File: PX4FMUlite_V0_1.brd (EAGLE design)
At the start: 70 x 40.5 mm, 192 parts, among them J201 DF13C-6P-1.25V, J202 DF13C-6P-1.25V, J203 DF13C-6P-1.25V, J204 DF13C-6P-1.25V, J301 47346-0001, J302 DF13C-4P-1.25V, J401 DF13C-4P-1.25V, J403 DF13C-7P-1.25V, J404 DF13C-5P-1.25V, J405 DF13C-4P-1.25V, J601 DF13C-6P-1.25V, J702 DF13C-3P-1.25V, J801 JST-ZH-3, M3_MOUNT1101 MOUNT-HOLE3.1MM, M3_MOUNT1102 MOUNT-HOLE3.1MM, M3_MOUNT1103 MOUNT-HOLE3.1MM, M3_MOUNT1104 MOUNT-HOLE3.1MM, U101 STM32F4X7VX, U102 FM25V01, U201 TXS0108QFN20, U202 TXS0108QFN20, U301 2908-05WB-MG, U401 MAX3051, U502 L3GD20H, U503 MS5611-01BA, U701 TCA62724FMG, U703 LRTB GFTG-T7AW-1+V7A7-29+R5T9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, U901 TXS0108QFN20, U903 74LVC2G240, X101 3.2x2.5 mm / 24 MHz / 15 ppm

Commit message: lots of ripus done on V0_1
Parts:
- moved R207 76.7 mm to (30.0, 82.0)
- moved C202 76.7 mm to (34.0, 83.6)
- moved J203 76.7 mm to (34.4, 83.6)
- moved JP2 76.7 mm to (29.0, 77.7)
- moved R214 76.7 mm to (31.2, 82.4)
- moved S3RX 76.7 mm to (31.6, 80.0)
- moved U202 76.7 mm to (34.0, 80.0)
- moved JX801 52.4 mm to (22.3, 53.5)
- moved R607 44.8 mm to (59.0, 72.0)
- moved L601 44.8 mm to (61.3, 73.2)
- moved L602 44.8 mm to (61.3, 74.6)
- moved L603 44.8 mm to (59.5, 68.8)
- moved R604 44.8 mm to (59.0, 73.2)
- moved R605 44.8 mm to (59.0, 74.6)
- moved R606 44.8 mm to (59.0, 70.9)
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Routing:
- net GNDX: track 96.4 -> 25.2 mm, vias 15 -> 0
- net VBUS: track 57.3 -> 0.10 mm, vias 4 -> 0
- net !GYRO_CS: track 56.8 -> 0.00 mm, vias 1 -> 0
- net ACCEL_DRDY: track 52.6 -> 0.00 mm, vias 2 -> 0
- net !BARO_CS: track 47.6 -> 0.00 mm, vias 1 -> 0
- net FMU-VDD_3V3: track 71.3 -> 24.7 mm, vias 10 -> 0
- net FMU-!RESET: track 45.7 -> 1.94 mm, vias 3 -> 0
- net GPIO_EXT_1: track 42.2 -> 0.10 mm, vias 2 -> 0
- net SPI_INT_SCK: track 43.7 -> 2.07 mm, vias 1 -> 0
- net BATT_VOLTAGE_SENS: track 42.2 -> 0.66 mm, vias 2 -> 0
- net SPI_EXT_SCK: track 41.4 -> 0.00 mm, vias 3 -> 0
- net SPI_INT_MOSI: track 43.2 -> 2.14 mm, vias 1 -> 0
- net SPI_EXT_MISO: track 40.5 -> 0.00 mm, vias 3 -> 0
- net SPI_INT_MISO: track 41.5 -> 1.28 mm, vias 1 -> 0
- net !SPI_EXT_NSS: track 40.0 -> 0.00 mm, vias 3 -> 0
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- removed copper zone on layer 15, net FMU-VDD_3V3
- removed copper zone on layer 16, net GNDX
- removed copper zone on layer 16, net RGB_LED_14
- removed copper zone on layer 16, net RGB_LED_3
- removed copper zone on layer 16, net RGB_LED_4
- removed copper zone on layer 1, net VBUS
- removed copper zone on layer 3, net VBUS
- removed copper zone on layer 15, net VDD_3V3_SENSORS
- removed copper zone on layer 1, net VDD_5V_BRICK
- removed copper zone on layer 16, net VDD_5V_BRICK
- removed copper zone on layer 1, net VDD_5V_IN
- removed copper zone on layer 15, net VDD_5V_IN
- removed copper zone on layer 16, net VDD_5V_IN
- removed copper zone on layer 1, net VDD_5V_PERIPH
- removed copper zone on layer 15, net VDD_5V_PERIPH
- removed copper zone on layer 1, net VDD_SERVO
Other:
- board size 70 x 40.5 mm -> 70 x 34.9 mm
- board text added: "PX4FMULite V0.1"
- board text removed: "PX4FMU v2.3"

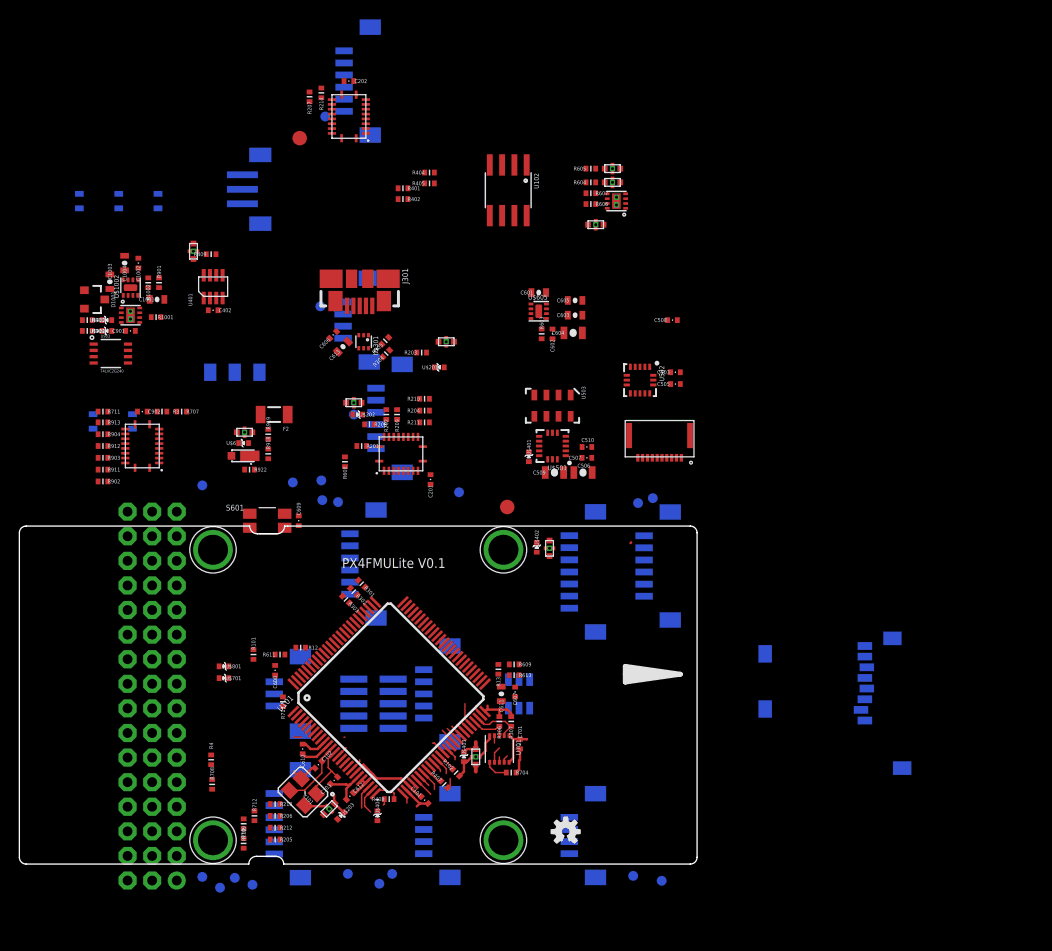
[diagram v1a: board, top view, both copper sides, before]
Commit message: Resize board, resized servo conn plus more
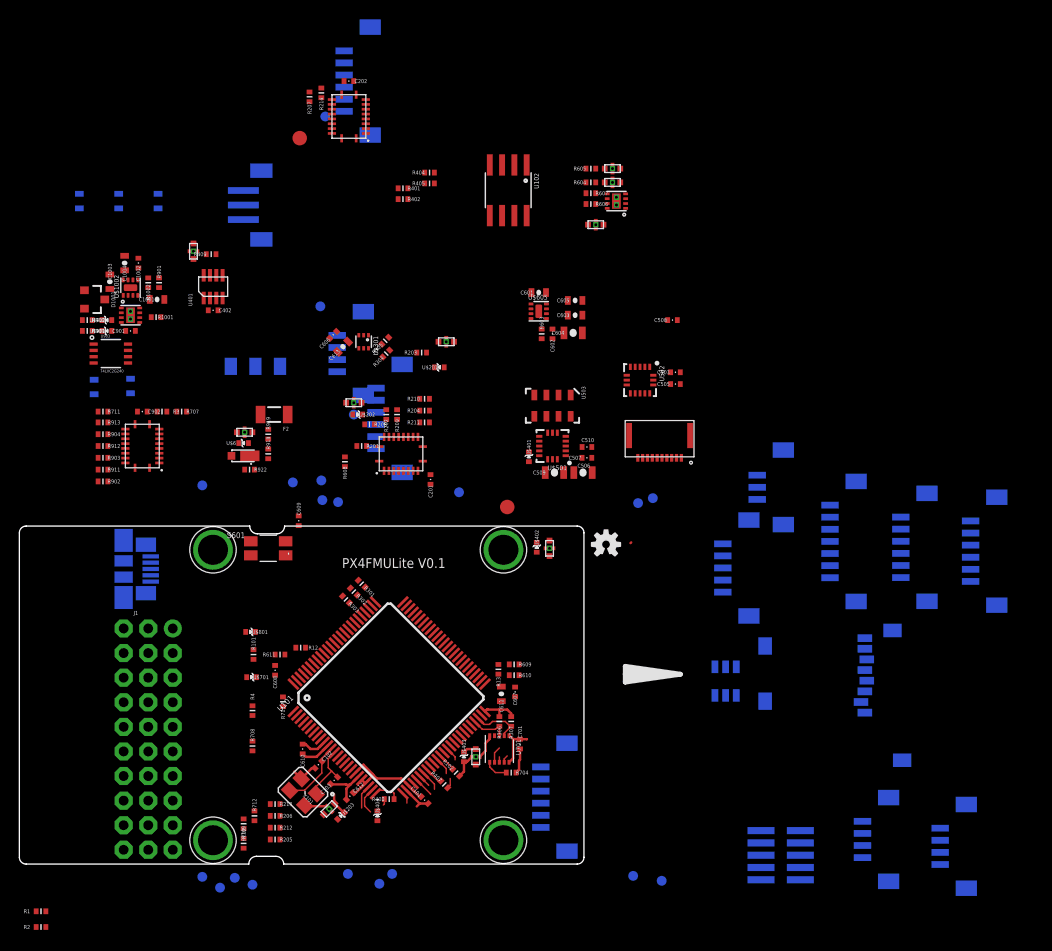
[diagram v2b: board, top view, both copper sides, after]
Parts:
- removed J901: (no value), pixhawk2:3X16RA
- added J1: (no value), PX4lite:3X10RA
- added R1, R2: 220R, pixhawk2:0402-RES
- moved J201 64.1 mm to (99.2, 35.1)
- moved J702 54.3 mm to (77.1, 41.7)
- moved J405 45.3 mm to (88.0, 5.28)
- moved JX301 44.9 mm to (78.6, 3.66)
- moved J301 38.6 mm to (10.8, 33.2), flipped to the bottom, turned to 180 degrees
- moved J401 38.3 mm to (96.0, 4.57)
- moved J404 33.5 mm to (73.6, 33.3)
- moved OSHW_LOGO 30.0 mm to (60.6, 35.8)
- moved J204 27.7 mm to (54.8, 9.65)
- moved J403 27.1 mm to (84.6, 36.1)
- moved J601 26.6 mm to (91.9, 35.5)
- moved U703 21.4 mm to (72.9, 21.6)
- moved R4 6.63 mm to (24.1, 18.6)
- moved R708 5.75 mm to (24.1, 14.9)
- moved U$801 4.49 mm to (23.9, 26.7)
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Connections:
- new net N$15: J1.22, R1.P$2
- new net N$16: J1.19, R2.P$2
- new net N$18: R1.P$1, U901.13
- new net N$21: R2.P$1, U901.12
- net FMU-CH1-PROT: now also J1.1; no longer J901.46
- net FMU-CH6-PROT: now also J1.16; no longer J901.31
- net GNDX: now also J1.12, J1.15, J1.18, J1.21, J1.24, J1.27, J1.3, J1.30, J1.6, J1.9; no longer J901.12, J901.15, J901.18, J901.21, J901.24, J901.27, J901.3, J901.30, J901.33, J901.36, J901.39, J901.42, J901.45, J901.48, J901.6, J901.9
- net IO-VDD_5V5: no longer J901.2
- net N$68: now also J1.13; no longer J901.34
- net N$77: now also J1.10; no longer J901.37
- net N$78: now also J1.7; no longer J901.40
- net N$79: now also J1.4; no longer J901.43
- net N$99: no longer J901.4
- net PPM-SBUS-PROT: no longer J901.1
- net VDD_SERVO: now also J1.11, J1.14, J1.17, J1.2, J1.20, J1.23, J1.26, J1.29, J1.5, J1.8; no longer J901.11, J901.14, J901.17, J901.20, J901.23, J901.26, J901.29, J901.32, J901.35, J901.38, J901.41, J901.44, J901.47, J901.5, J901.8
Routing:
- net !VDD_5V_PERIPH_OC: track 2.49 -> 0.00 mm
- net FMU-!RESET: track 1.94 -> 0.00 mm
- net !VDD_5V_HIPOWER_OC: track 1.75 -> 0.00 mm
- net FMU-UART7_RX: track 1.59 -> 0.00 mm
- net FMU-CH3: track 1.52 -> 0.00 mm
- net FMU_AUX_ADC1: track 2.03 -> 0.65 mm
- net !FMU-LED_AMBER: track 1.32 -> 0.00 mm
- net N$12: track 1.21 -> 0.00 mm
- net GYRO_DRDY: track 1.19 -> 0.00 mm
- net VDD_5V_SENS: track 1.18 -> 0.00 mm
- net FMU-CH2: track 1.09 -> 0.00 mm
- net FMU-CH1: track 0.87 -> 0.00 mm
- net VBAT: track 0.84 -> 0.00 mm
- net VDD_5V_PERIPH: track 0.72 -> 0.00 mm
- net N$98: track 2.07 -> 1.34 mm
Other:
- board size 70 x 34.9 mm -> 58.3 x 34.9 mm

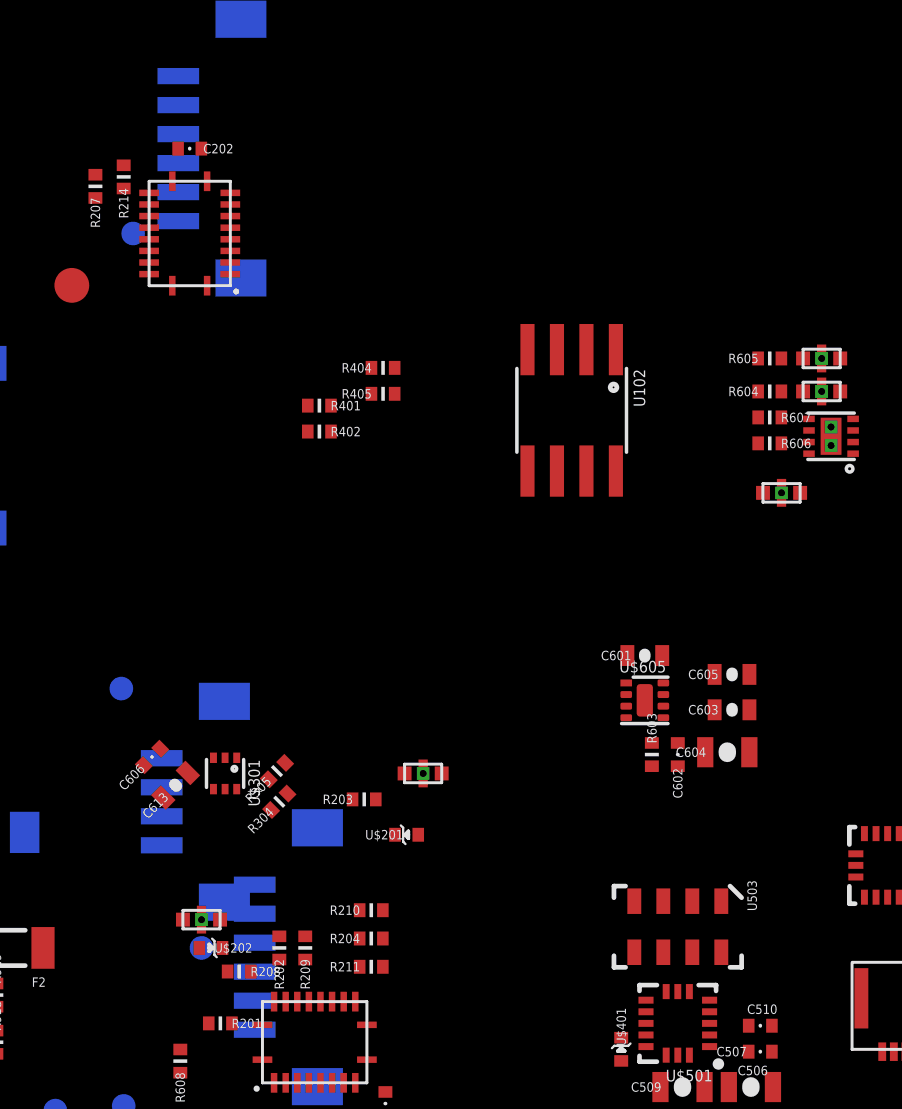
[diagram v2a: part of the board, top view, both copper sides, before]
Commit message: Removed TXS0105 buffer on excess uarts
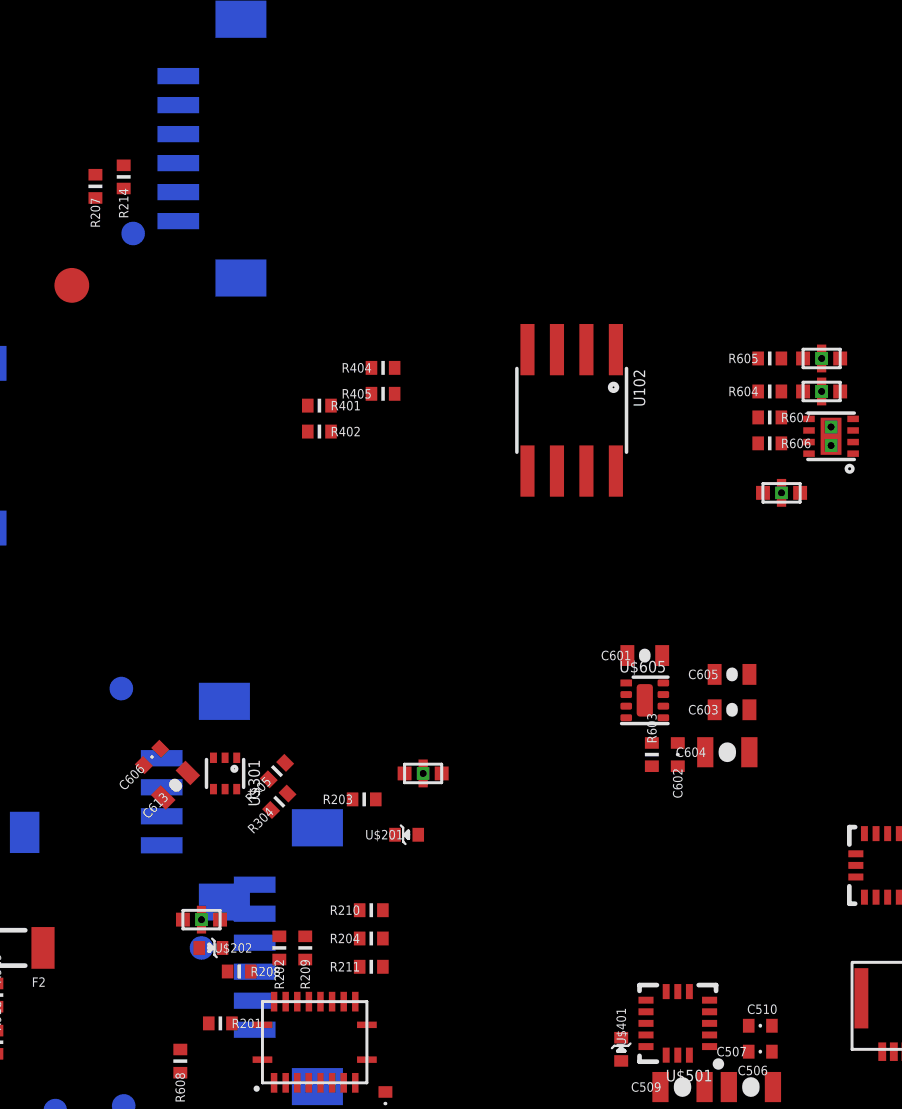
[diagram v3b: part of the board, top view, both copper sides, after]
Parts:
- removed C202: 0u1, pixhawk2:0402-CAP
- removed U202: TXS0108QFN20, pixhawk2:QFN20-RGY
- removed U503: MS5611-01BA, pixhawk2:MS5611-01BA
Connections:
- removed net N$90: R214.P$1, U202.12
- removed net N$91: R205.P$1, U202.17
- removed net N$92: R212.P$1, U202.16
- removed net N$93: R206.P$1, U202.15
- removed net N$94: R213.P$1, U202.14
- net !BARO_CS: no longer U503.5
- net FMU-UART4_RX: no longer U202.8
- net FMU-UART4_TX: now also R214.P$1; no longer U202.9
- net FMU-UART7_RX: now also R205.P$1; no longer U202.4
- net FMU-UART7_TX: now also R212.P$1; no longer U202.5
- net FMU-UART8_RX: now also R206.P$1; no longer U202.6
- net FMU-UART8_TX: now also R213.P$1; no longer U202.7
- net FMU-VDD_3V3: no longer C202.P$1, U202.10, U202.19, U202.2
- net GNDX: no longer C202.P$2, U202.11, U503.2, U503.3
- net N$89: no longer U202.13
- net SPI_INT_MISO: no longer U503.6
- net SPI_INT_MOSI: no longer U503.7
- net SPI_INT_SCK: no longer U503.8
- net VDD_3V3_SENSORS: no longer U503.1

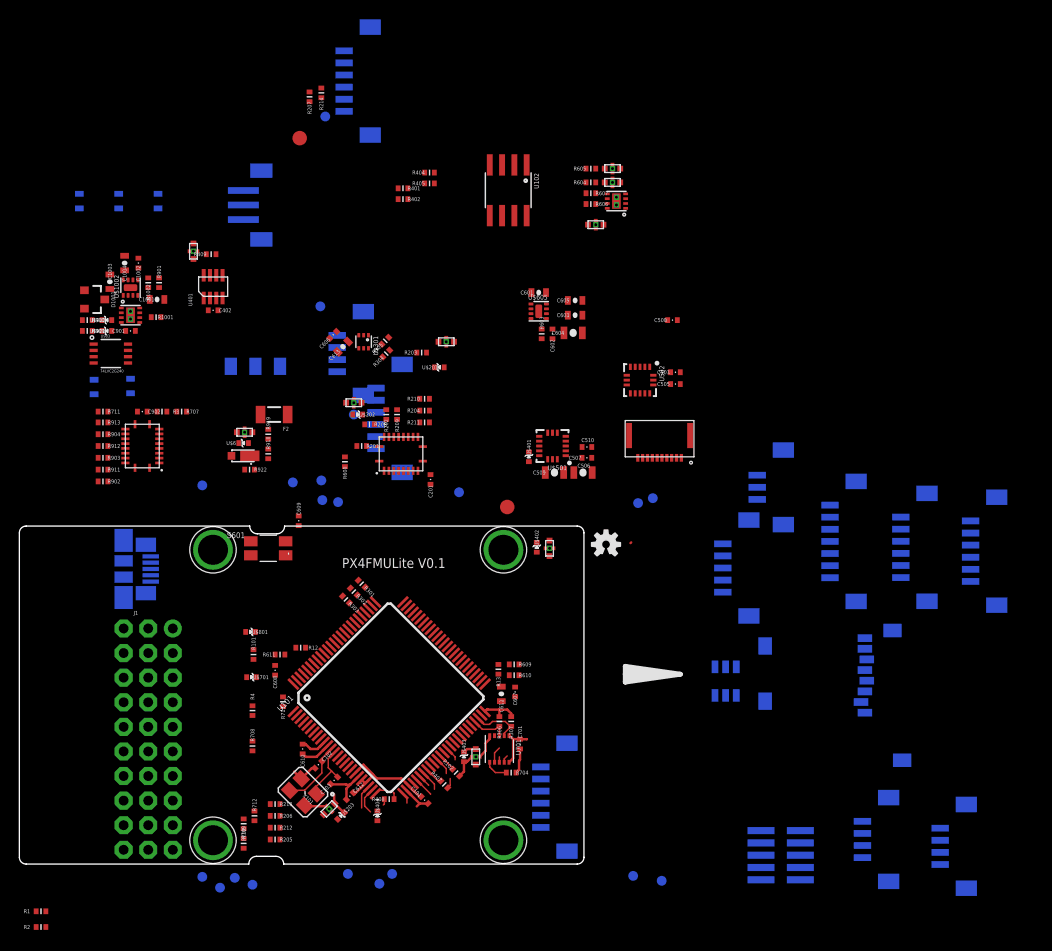
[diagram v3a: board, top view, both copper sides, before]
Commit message: Replaced lvl translators with NFU8042 ESD/EMI filters
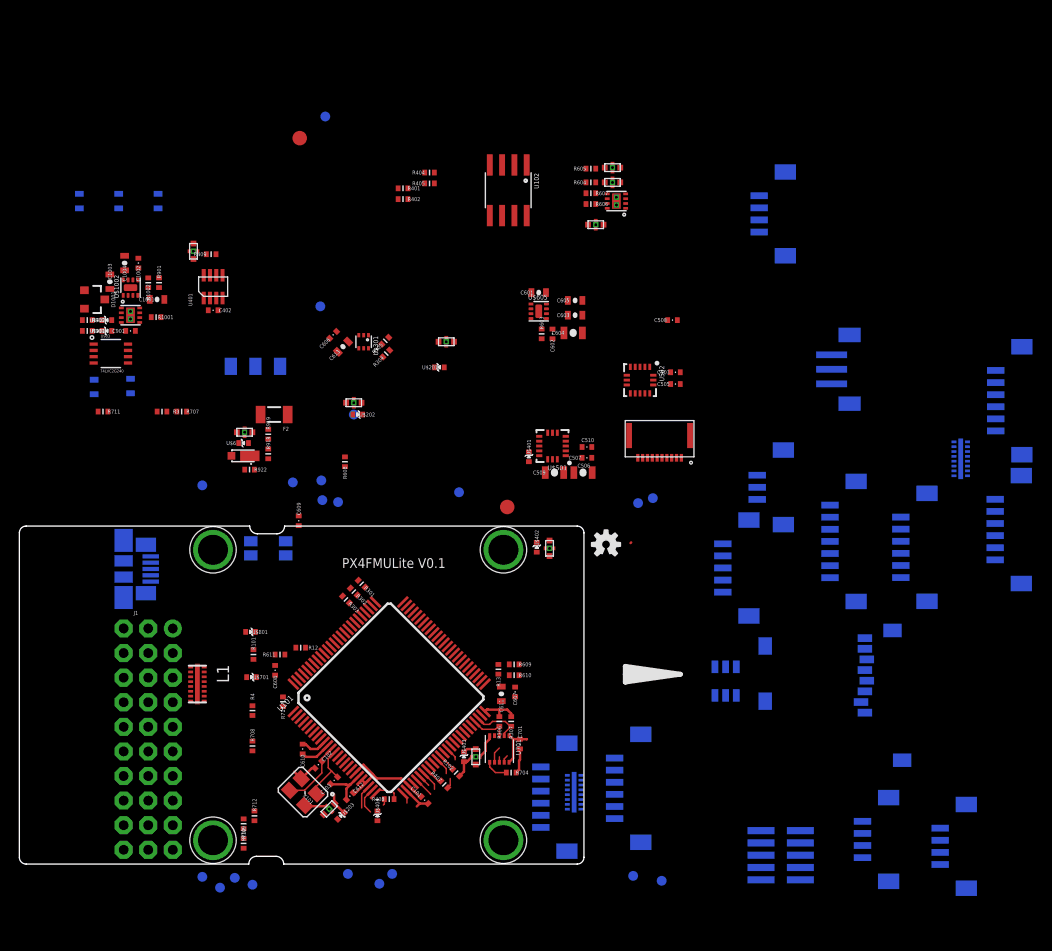
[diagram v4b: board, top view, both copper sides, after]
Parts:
- removed C201, C902: 0u1, pixhawk2:0402-CAP
- removed R1, R2, R902, R903, R904, R911, R912, R913: 220R, pixhawk2:0402-RES
- removed R201, R202, R203, R204, R205, R206, R207, R208, R209, R210, R211, R212, R213, R214: 120R, pixhawk2:0402-RES
- removed U201, U901: TXS0108QFN20, pixhawk2:QFN20-RGY
- added L1, L2, L3: NUF8402MN, PX4lite:DFN16-THIN
- moved J203 78.2 mm to (62.4, 10.6)
- moved J202 64.0 mm to (101.7, 50.6)
- moved J801 63.1 mm to (85.6, 53.8)
- moved J302 45.9 mm to (77.3, 69.9)
- moved J201 3.38 mm to (101.7, 37.3)
- moved L602 0.10 mm to (61.3, 74.7)
- flipped S601 to the bottom
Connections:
- removed net FMU-CH6-PROT: J1.16, R902.P$2
- removed net N$18: R1.P$1, U901.13
- removed net N$21: R2.P$1, U901.12
- removed net N$61: R902.P$1, U901.20
- removed net N$62: R911.P$1, U901.18
- removed net N$63: R903.P$1, U901.17
- removed net N$64: R912.P$1, U901.16
- removed net N$65: R904.P$1, U901.15
- removed net N$66: R913.P$1, U901.14
- removed net N$70: R201.P$1, U201.20
- removed net N$82: R208.P$1, U201.18
- removed net N$83: R202.P$1, U201.17
- removed net N$84: R209.P$1, U201.16
- removed net N$85: R203.P$1, U201.15
- removed net N$86: R210.P$1, U201.14
- removed net N$87: R204.P$1, U201.13
- removed net N$88: R211.P$1, U201.12
- removed net N$89: R207.P$1
- new net N$32: L1.P$7
- new net N$36: J1.16, L1.P$11
- net FMU-CH1: no longer U901.7
- net FMU-CH1-PROT: now also L1.P$16; no longer R913.P$2
- net FMU-CH2: no longer U901.6
- net FMU-CH3: no longer U901.5
- net FMU-CH4: no longer U901.4
- net FMU-CH5: no longer U901.3
- net FMU-CH6: no longer U901.1
- net FMU-UART4_RX: now also L3.P$5
- net FMU-UART4_TX: now also L3.P$6; no longer R214.P$1
- net FMU-UART7_RX: now also L3.P$1; no longer R205.P$1
- net FMU-UART7_TX: now also L3.P$2; no longer R212.P$1
- net FMU-UART8_RX: now also L3.P$3; no longer R206.P$1
- net FMU-UART8_TX: now also L3.P$4; no longer R213.P$1
- net FMU-USART2_CTS: now also L2.P$8; no longer U201.9
- net FMU-USART2_RTS: now also L2.P$7; no longer U201.8
- net FMU-USART2_RX: now also L2.P$5; no longer U201.6
- net FMU-USART2_TX: now also L2.P$6; no longer U201.7
- net FMU-USART3_CTS: now also L2.P$2; no longer U201.3
- net FMU-USART3_RTS: now also L2.P$1; no longer U201.1
- net FMU-USART3_RX: now also L2.P$3; no longer U201.4
- net FMU-USART3_TX: now also L2.P$4; no longer U201.5
- net FMU-VDD_3V3: no longer C201.P$1, C902.P$1, U201.10, U201.19, U201.2, U901.10, U901.19, U901.2
- net GNDX: now also L1.P$EP, L2.P$EP, L3.P$EP; no longer C201.P$2, C902.P$2, U201.11, U901.11
- net N$15: now also L1.P$9; no longer R1.P$2
- net N$16: no longer R2.P$2
- net N$68: no longer R911.P$2
- net N$77: now also L1.P$13; no longer R903.P$2
- net N$78: now also L1.P$14; no longer R912.P$2
- net N$79: now also L1.P$15; no longer R904.P$2
- net SERIAL1_CTS: now also L2.P$9; no longer R211.P$2
- net SERIAL1_RTS: now also L2.P$10; no longer R204.P$2
- net SERIAL1_RX: now also L2.P$12; no longer R203.P$2
- net SERIAL1_TX: now also L2.P$11; no longer R210.P$2
- net SERIAL2_CTS: now also L2.P$15; no longer R208.P$2
- net SERIAL2_RTS: now also L2.P$16; no longer R201.P$2
- net SERIAL2_RX: now also L2.P$14; no longer R202.P$2
- net SERIAL2_TX: now also L2.P$13; no longer R209.P$2
- net SERIAL3_RX: now also L3.P$12; no longer R207.P$2
- net SERIAL3_TX: now also L3.P$11; no longer R214.P$2
- net SERIAL4_RX: now also L3.P$14; no longer R206.P$2
- net SERIAL4_TX: now also L3.P$13; no longer R213.P$2
- net SERIAL5_RX: now also L3.P$16; no longer R205.P$2
- net SERIAL5_TX: now also L3.P$15; no longer R212.P$2
